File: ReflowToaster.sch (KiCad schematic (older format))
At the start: 3 parts, among them J2 USB-Micro-B, J3 USB-Micro-B, Q1 FDN340P

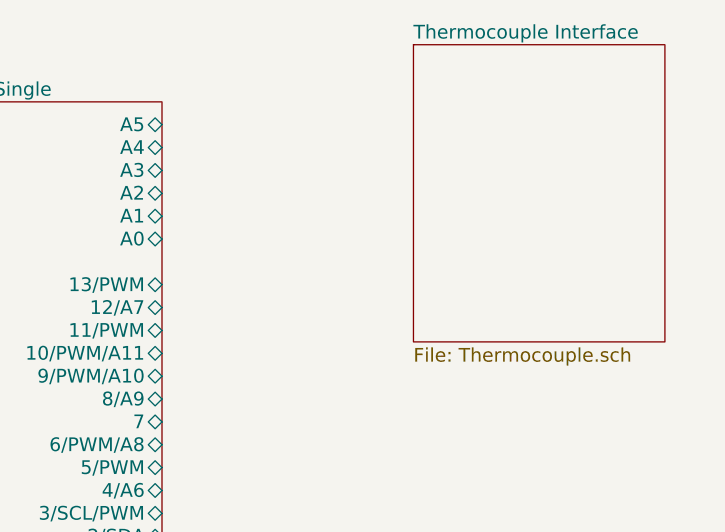
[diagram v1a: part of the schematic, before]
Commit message: thermocouple section complete
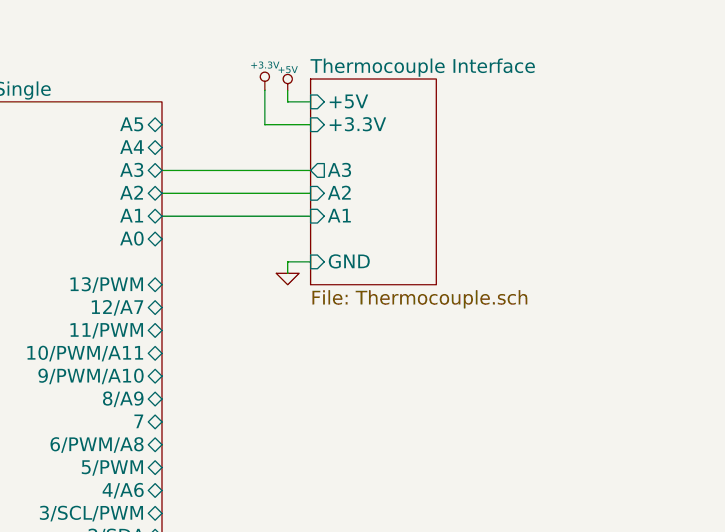
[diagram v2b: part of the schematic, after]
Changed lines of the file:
@@
 LIBS:74xgxx
 LIBS:74xx
+LIBS:conn
 LIBS:ReflowToaster-cache
 EELAYER 24 0
@@
 $EndComp
 $Sheet
-S 5100 2450 1100 1300
+S 4650 2600 550  900
 U 540FBA95
 F0 "Thermocouple Interface" 60
 F1 "Thermocouple.sch" 60
+F2 "A3" O L 4650 3000 60
+F3 "A1" I L 4650 3200 60
+F4 "A2" I L 4650 3100 60
+F5 "+5V" I L 4650 2700 60
+F6 "+3.3V" I L 4650 2800 60
+F7 "GND" I L 4650 3400 60
 $EndSheet
+Wire Wire Line
+	4000 3000 4650 3000
+Wire Wire Line
+	4650 3100 4000 3100
+Wire Wire Line
+	4000 3200 4650 3200
+$Comp
+L GND #PWR08
+U 1 1 5410CA3E
+P 4550 3450
+F 0 "#PWR08" H 4550 3450 30  0001 C CNN
+F 1 "GND" H 4550 3380 30  0001 C CNN
+F 2 "" H 4550 3450 60  0000 C CNN
+F 3 "" H 4550 3450 60  0000 C CNN
+	1    4550 3450
+	1    0    0    -1
+$EndComp
+$Comp
+L +3.3V #PWR09
+U 1 1 5410CC8C
+P 4450 2650
+F 0 "#PWR09" H 4450 2610 30  0001 C CNN
+F 1 "+3.3V" H 4450 2760 30  0000 C CNN
+F 2 "" H 4450 2650 60  0000 C CNN
+F 3 "" H 4450 2650 60  0000 C CNN
+	1    4450 2650
+	1    0    0    -1
+$EndComp
+$Comp
+L +5V #PWR010
+U 1 1 5410CCA0
+P 4550 2650
+F 0 "#PWR010" H 4550 2740 20  0001 C CNN
+F 1 "+5V" H 4550 2740 30  0000 C CNN
+F 2 "" H 4550 2650 60  0000 C CNN
+F 3 "" H 4550 2650 60  0000 C CNN
+	1    4550 2650
+	1    0    0    -1
+$EndComp
+Wire Wire Line
+	4550 2650 4550 2700
+Wire Wire Line
+	4550 2700 4650 2700
+Wire Wire Line
+	4650 2800 4450 2800
+Wire Wire Line
+	4450 2800 4450 2650
+Wire Wire Line
+	4550 3450 4550 3400
+Wire Wire Line
+	4550 3400 4650 3400
 $EndSCHEMATC

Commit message: schematic complete
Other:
- moved on the sheet: J2, J3, Q1

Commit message: DuinoModSingle & main sheet tagged with vendor part #s for BOM generation
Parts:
- J2, J3: DigiKey P/N (none) -> 609-4613-1-ND; Mouser P/N (none) -> 649-10118192-0001LF
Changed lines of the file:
@@
 F 4 "FCI" H 3500 4600 60  0001 C CNN "Manufacturer"
 F 5 "10118192-0001LF" H 3500 4600 60  0001 C CNN "Part Number"
-F 6 "Power and Data" H 3500 4150 60  0000 C CNN "Usage"
+F 6 "609-4613-1-ND" H 0   0   50  0001 C CNN "DigiKey P/N"
+F 7 "649-10118192-0001LF" H 0   0   50  0001 C CNN "Mouser P/N"
+F 8 "Power and Data" H 3500 4150 60  0000 C CNN "Usage"
 	1    3500 4600
 	-1   0    0    -1
@@
 F 4 "FCI" H 3500 3550 60  0001 C CNN "Manufacturer"
 F 5 "10118192-0001LF" H 3500 3550 60  0001 C CNN "Part Number"
-F 6 "Power Only" H 3500 3100 60  0000 C CNN "Usage"
+F 6 "609-4613-1-ND" H 0   0   50  0001 C CNN "DigiKey P/N"
+F 7 "649-10118192-0001LF" H 0   0   50  0001 C CNN "Mouser P/N"
+F 8 "Power Only" H 3500 3100 60  0000 C CNN "Usage"
 	1    3500 3550
 	-1   0    0    -1

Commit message: components tagged with vendor part IDs
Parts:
- Q1: DigiKey P/N (none) -> FDN340PCT-ND; Mouser P/N (none) -> 512-FDN340P
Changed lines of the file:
@@
 F 1 "FDN340P" V 4550 4400 60  0000 R CNN
 F 2 "ReflowToaster:FDN340P" H 4400 5150 60  0001 C CNN
-F 3 "http://datasheet.octopart.com/FDN340P-Fairchild-datasheet-31668.pdf" H 4400 5250 60  0001 C CNN
+F 3 "http://www.fairchildsemi.com/datasheets/FD/FDN340P.pdf" H 4400 5250 60  0001 C CNN
 F 4 "Fairchild" H 4400 5350 60  0001 C CNN "Manufacturer"
 F 5 "FDN340P" H 4400 5450 60  0001 C CNN "Part Number"
+F 6 "FDN340PCT-ND" H 0   0   50  0001 C CNN "DigiKey P/N"
+F 7 "512-FDN340P" H 0   0   50  0001 C CNN "Mouser P/N"
 	1    4400 4200
 	0    -1   1    0

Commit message: redo annotation
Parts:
- renumbered J3 to J1
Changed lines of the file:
@@
 $EndComp
 $Comp
-L GND #PWR01
+L GND #PWR4
 U 1 1 540F85D9
 P 4100 4950
-F 0 "#PWR01" H 4100 4950 30  0001 C CNN
+F 0 "#PWR4" H 4100 4950 30  0001 C CNN
 F 1 "GND" H 4100 4880 30  0001 C CNN
 F 2 "" H 4100 4950 60  0000 C CNN
@@
 $EndComp
 $Comp
-L GND #PWR02
+L GND #PWR2
 U 1 1 540F86BE
 P 2900 4900
-F 0 "#PWR02" H 2900 4900 30  0001 C CNN
+F 0 "#PWR2" H 2900 4900 30  0001 C CNN
 F 1 "GND" H 2900 4830 30  0001 C CNN
 F 2 "" H 2900 4900 60  0000 C CNN
@@
 $EndComp
 $Comp
-L USB-Micro-B J3
+L USB-Micro-B J1
 U 1 1 540F90B7
 P 3500 3550
-F 0 "J3" H 3250 4000 60  0000 C CNN
+F 0 "J1" H 3250 4000 60  0000 C CNN
 F 1 "USB-Micro-B" H 3450 3050 60  0001 C CNN
 F 2 "ReflowToaster:FCI_10118192-0001LF" H 3500 3550 60  0001 C CNN
@@
 $EndComp
 $Comp
-L GND #PWR03
+L GND #PWR3
 U 1 1 540F9794
 P 4100 3900
-F 0 "#PWR03" H 4100 3900 30  0001 C CNN
+F 0 "#PWR3" H 4100 3900 30  0001 C CNN
 F 1 "GND" H 4100 3830 30  0001 C CNN
 F 2 "" H 4100 3900 60  0000 C CNN
@@
 $EndComp
 $Comp
-L GND #PWR04
+L GND #PWR1
 U 1 1 540F97A8
 P 2900 3850
-F 0 "#PWR04" H 2900 3850 30  0001 C CNN
+F 0 "#PWR1" H 2900 3850 30  0001 C CNN
 F 1 "GND" H 2900 3780 30  0001 C CNN
 F 2 "" H 2900 3850 60  0000 C CNN
@@
 $EndComp
 $Comp
-L GND #PWR05
+L GND #PWR7
 U 1 1 540F9DBA
 P 4600 5550
-F 0 "#PWR05" H 4600 5550 30  0001 C CNN
+F 0 "#PWR7" H 4600 5550 30  0001 C CNN
 F 1 "GND" H 4600 5480 30  0001 C CNN
 F 2 "" H 4600 5550 60  0000 C CNN
@@
 $EndComp
 $Comp
-L +5V #PWR06
+L +5V #PWR6
 U 1 1 540F9FAE
 P 4600 2950
-F 0 "#PWR06" H 4600 3040 20  0001 C CNN
+F 0 "#PWR6" H 4600 3040 20  0001 C CNN
 F 1 "+5V" H 4600 3040 30  0000 C CNN
 F 2 "" H 4600 2950 60  0000 C CNN
@@
 $EndComp
 $Comp
-L +3.3V #PWR07
+L +3.3V #PWR5
 U 1 1 540F9FC2
 P 4450 2950
-F 0 "#PWR07" H 4450 2910 30  0001 C CNN
+F 0 "#PWR5" H 4450 2910 30  0001 C CNN
 F 1 "+3.3V" H 4450 3060 30  0000 C CNN
 F 2 "" H 4450 2950 60  0000 C CNN
@@
 $EndSheet
 $Comp
-L GND #PWR08
+L GND #PWR10
 U 1 1 5410CA3E
 P 6800 2900
-F 0 "#PWR08" H 6800 2900 30  0001 C CNN
+F 0 "#PWR10" H 6800 2900 30  0001 C CNN
 F 1 "GND" H 6800 2830 30  0001 C CNN
 F 2 "" H 6800 2900 60  0000 C CNN
@@
 $EndComp
 $Comp
-L +3.3V #PWR09
+L +3.3V #PWR8
 U 1 1 5410CC8C
 P 6700 2100
-F 0 "#PWR09" H 6700 2060 30  0001 C CNN
+F 0 "#PWR8" H 6700 2060 30  0001 C CNN
 F 1 "+3.3V" H 6700 2210 30  0000 C CNN
 F 2 "" H 6700 2100 60  0000 C CNN
@@
 $EndComp
 $Comp
-L +5V #PWR010
+L +5V #PWR9
 U 1 1 5410CCA0
 P 6800 2100
-F 0 "#PWR010" H 6800 2190 20  0001 C CNN
+F 0 "#PWR9" H 6800 2190 20  0001 C CNN
 F 1 "+5V" H 6800 2190 30  0000 C CNN
 F 2 "" H 6800 2100 60  0000 C CNN
@@
 $EndSheet
 $Comp
-L +5V #PWR011
+L +5V #PWR11
 U 1 1 54119BA4
 P 6800 3250
-F 0 "#PWR011" H 6800 3340 20  0001 C CNN
+F 0 "#PWR11" H 6800 3340 20  0001 C CNN
 F 1 "+5V" H 6800 3340 30  0000 C CNN
 F 2 "" H 6800 3250 60  0000 C CNN
@@
 $EndComp
 $Comp
-L GND #PWR012
+L GND #PWR12
 U 1 1 54119F4E
 P 6800 4850
-F 0 "#PWR012" H 6800 4850 30  0001 C CNN
+F 0 "#PWR12" H 6800 4850 30  0001 C CNN
 F 1 "GND" H 6800 4780 30  0001 C CNN
 F 2 "" H 6800 4850 60  0000 C CNN
